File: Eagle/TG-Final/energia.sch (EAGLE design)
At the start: 1 part

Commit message: Comienzo placa potencia
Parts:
- added C1: 470uf, rcl:CPOL-USE3.5-8
- added C2: 0.1uf, rcl:C-EU025-025X050
- added D1: 1N4007, adafruit:1N4004
- added IC1, IC2: 7812T, linear:7812T
- added IC3: 7806T, linear:7806T
- added R1, R2: 1 Ohm 1W, rcl:R-US_0411/15
- added U$8: PIC16F88-DIP, SparkFun:PIC16F88-DIP
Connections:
- net P$1 renamed +11V1
- removed net +24V: U$1.PIN17
- removed net +5V: U$1.PIN20
- new net +22V: R1.1, R2.1, U$1.PIN17
- new net +6V: IC3.VO, U$1.PIN20
- new net N$1: IC2.VI, R2.2
- new net N$2: D1.C, IC1.VI, R1.2
- new net VDD: U$1.PIN21
- net +12V: now also C1.+, C2.1, D1.A, IC1.VO, IC2.VO, IC3.VI
- net +3V3: now also U$1.PIN22; no longer U$1.PIN21
- net VSS: now also C1.-, C2.2, IC1.GND, IC2.GND, IC3.GND

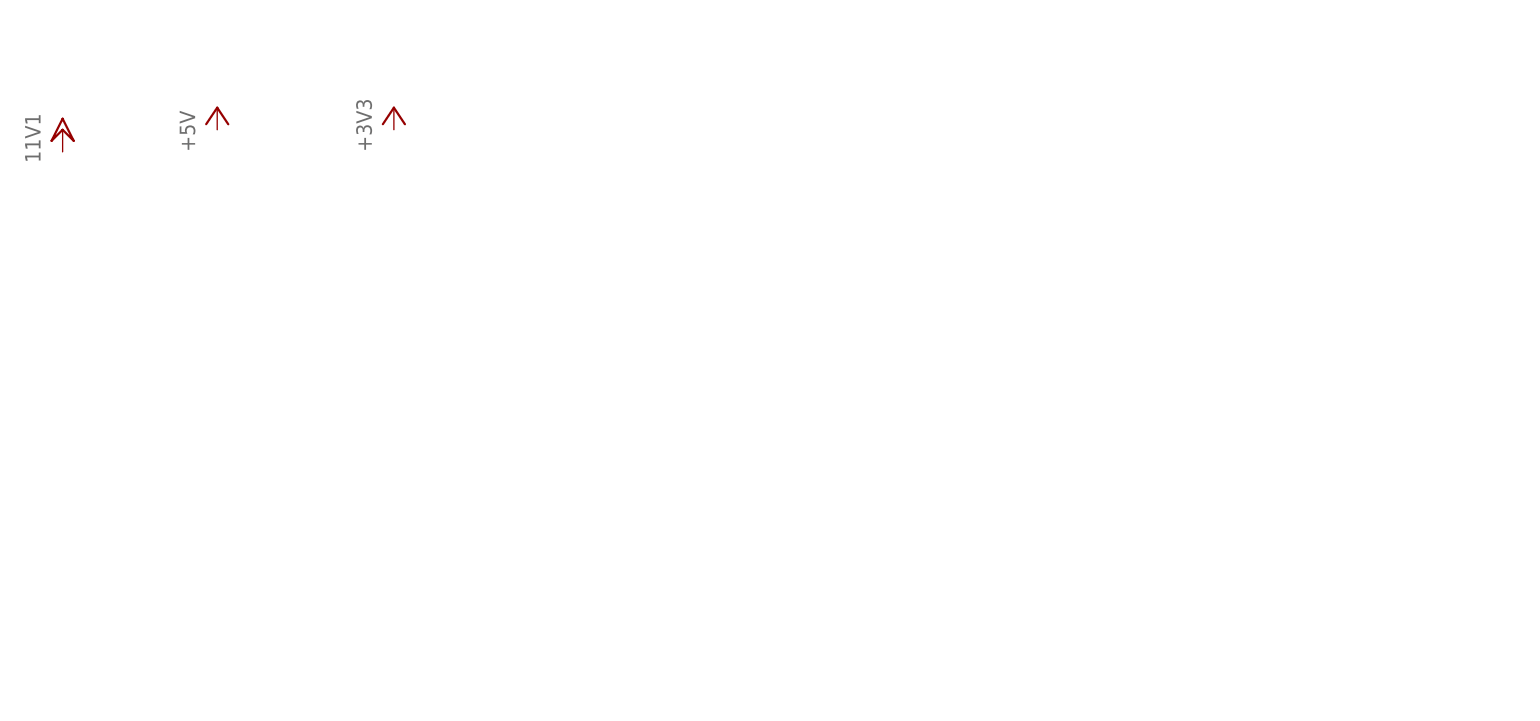
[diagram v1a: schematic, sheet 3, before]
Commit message: Fuente 11.1v -> 5v y 3v3
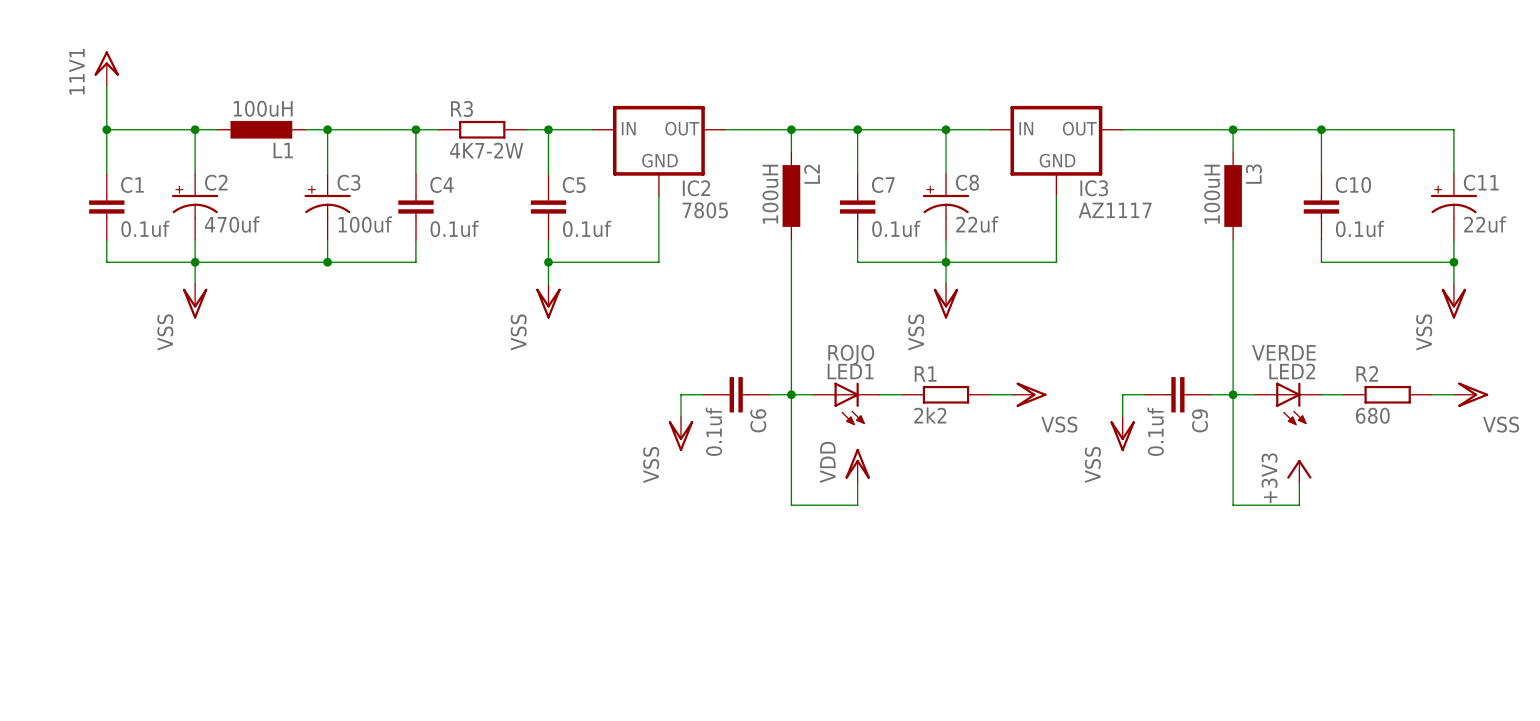
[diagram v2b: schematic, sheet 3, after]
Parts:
- removed D1: 1N4007, adafruit:1N4004
- added C10, C4, C5, C6, C7, C9: 0.1uf, rcl:C-EU050-024X044
- added C11, C8: 22uf, rcl:CPOL-USE2.5-7
- added C3: 100uf, rcl:CPOL-USE2.5-7
- added JP1: (no value), SparkFun:M06LONGPADS
- added L1, L2, L3: 100uH, rcl:L-EU0207/7
- added LED1: ROJO, adafruit:LED3MM
- added LED2: VERDE, adafruit:LED3MM
- added Q1: TIP2955, transistor-power:TIP2955
- added R3: 4K7-2W, rcl:R-EU_0411/12
- C1: value 470uf -> 0.1uf; device rcl:CPOL-USE3.5-8 -> rcl:C-EU050-024X044
- C2: value 0.1uf -> 470uf; device rcl:C-EU025-025X050 -> rcl:CPOL-USE2.5-7
- IC2: value 7812T -> 7805; device linear:7812T -> SparkFun:V_REG_78XX-TO-220
- IC3: value 7806T -> AZ1117; device linear:7806T -> SparkFun:V_REG_LD1117VXX
- R1: value 1 Ohm 1W -> 2k2; device rcl:R-US_0411/15 -> rcl:R-EU_0204/5
- R2: value 1 Ohm 1W -> 680; device rcl:R-US_0411/15 -> rcl:R-EU_0204/5
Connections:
- new net N$10: C5.1, IC2.IN, R3.2
- new net N$11: C3.+, C4.1, L1.2, R3.1
- new net N$12: C7.1, C8.+, IC2.OUT, IC3.IN, L2.2
- new net N$14: LED1.C, R1.1
- new net N$17: C10.1, C11.+, IC3.OUT, L3.2
- new net N$18: LED2.C, R2.1
- new net N$3: JP1.5, U$8.VDD
- new net N$4: JP1.4, U$8.VSS
- new net N$5: JP1.3, U$8.RB7/PGD
- new net N$6: JP1.2, U$8.RB6/PGC
- new net N$7: U$1.PIN15
- new net N$8: U$1.PIN14
- new net N$9: U$1.PIN13
- net +11V1: now also C1.1, C2.+, L1.1
- net +12V: no longer C1.+, C2.1, D1.A, IC1.VO, IC2.VO, IC3.VI
- net +22V: now also IC1.VI, Q1.B, Q1.E; no longer R1.1, R2.1
- net +3V3: now also C9.1, L3.1, LED2.A
- net +6V: no longer IC3.VO
- net N$1: now also IC1.VO, Q1.C; no longer IC2.VI, R2.2
- net N$2: now also JP1.6, U$8.RA5/MCLR; no longer D1.C, IC1.VI, R1.2
- net VDD: now also C6.1, L2.1, LED1.A
- net VSS: now also C1.2, C10.2, C11.-, C2.-, C3.-, C4.2, C5.2, C6.2, C7.2, C8.-, C9.2, R1.2, R2.2; no longer C1.-, C2.2
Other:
- moved on the sheet: IC1, U$8

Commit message: Monitor Baterias LiPO
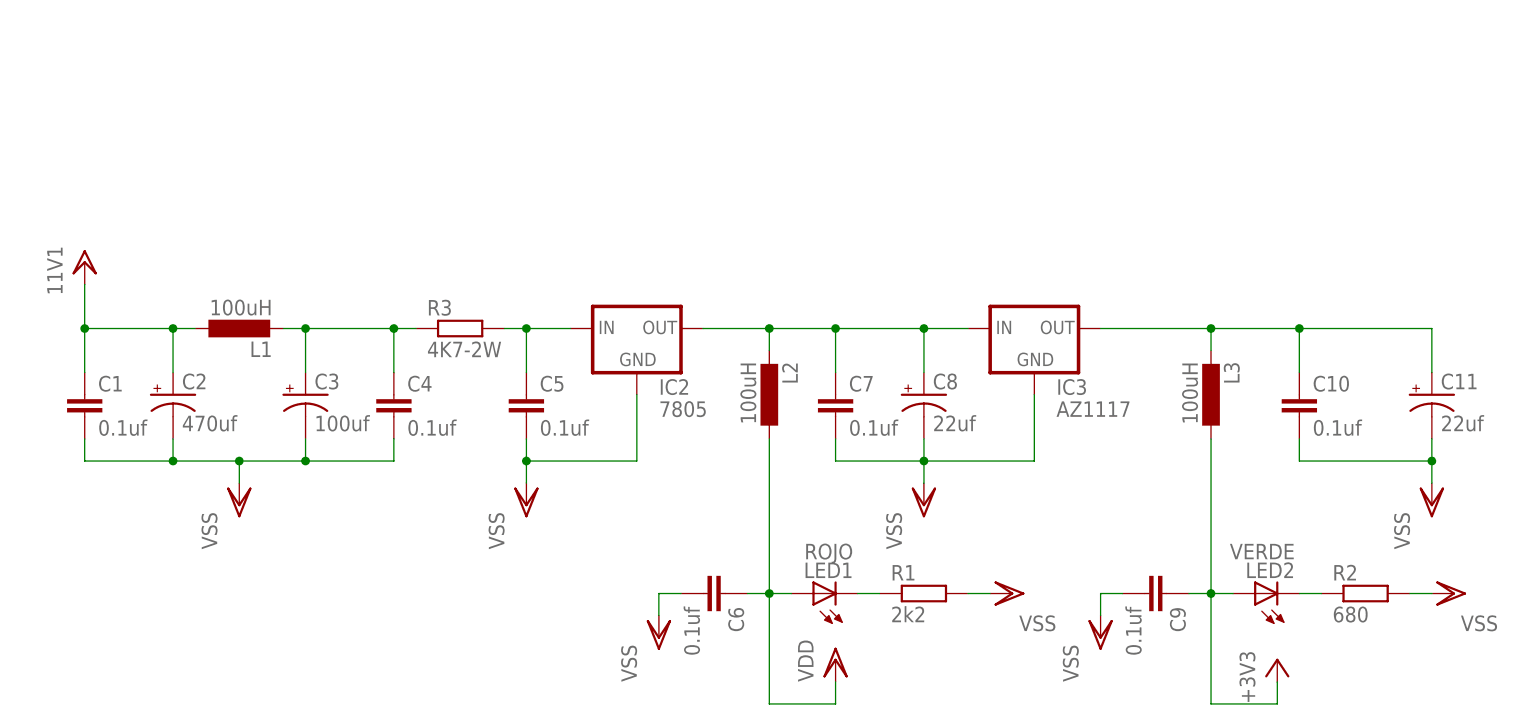
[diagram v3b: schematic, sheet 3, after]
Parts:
- removed IC1: 7812T, linear:7812T
- removed Q1: TIP2955, transistor-power:TIP2955
- added R4: 1k, rcl:R-EU_0204/5
- JP1: value (none) -> (none)
- renumbered U$8 to MONITORBATERIA
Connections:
- removed net N$1: IC1.VO, Q1.C
- removed net N$3: JP1.5, MONITORBATERIA.VDD
- removed net N$4: JP1.4, MONITORBATERIA.VSS
- removed net N$7: U$1.PIN15
- removed net N$8: U$1.PIN14
- removed net N$9: U$1.PIN13
- new net SENSE1: MONITORBATERIA.RA0/AN0, U$1.PIN15
- new net SENSE2: MONITORBATERIA.RA1/AN1, U$1.PIN13
- new net SENSE3: MONITORBATERIA.RA2/AN2, U$1.PIN14
- net +22V: no longer IC1.VI, Q1.B, Q1.E
- net VDD: now also JP1.5, MONITORBATERIA.VDD, R4.1
- net VSS: now also JP1.4, MONITORBATERIA.VSS, R4.2; no longer IC1.GND
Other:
- moved on the sheet: C1, C10, C11, C2, C3, C4, C5, C6, C7, C8, C9, IC2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

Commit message: Fuente de Potencia
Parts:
- removed R3: 4K7-2W, rcl:R-EU_0411/12
- added C12: 3300uf, rcl:CPOL-USE7.5-18
- added C13, C15: 470uf, rcl:CPOL-USE3.5-8
- added C14: 10uf, rcl:CPOL-USE2.5-5
- added C16, C17: 0.1uf, rcl:C-EU050-024X044
- added D1: 1N4007, diode:1N4004
- added IC1: 7812T, adafruit:7812T
- added IC4: 7806T, adafruit:7806T
- added Q1: TIP2955, transistor-power:TIP2955
- added R5: 2W100R, rcl:R-EU_0411/12
- added S1: SWITCH-2-ESTADOS, aasanchez:TL39YOSWITCH_2_ESTADOS
- added S2: SWITCH, aasanchez:TL39YOSWITCH_2_ESTADOS
- added U$6: 5W0.1RJ, aasanchez:RESISTENCIA5WATT
- added U$9: 10W 5R6J, aasanchez:RESISTENCIA10W
- L1: device rcl:L-EU0207/7 -> rcl:L-EUTFI0307
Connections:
- new net N$1: C1.1, C2.+, L1.1, S1.P
- new net N$13: C15.+, C16.1, D1.C, IC4.VI
- new net N$4: C12.+, R5.1, S2.P, U$6.P$1
- new net N$7: Q1.E, U$6.P$2
- new net N$8: C13.+, IC1.VI, Q1.B, R5.2
- net +11V1: now also S1.O; no longer C1.1, C2.+, L1.1
- net +12V: now also C14.+, D1.A, IC1.VO, Q1.C
- net +22V: now also S2.O
- net +6V: now also C17.1, IC4.VO
- net N$10: now also U$9.P$2; no longer R3.2
- net N$11: now also U$9.P$1; no longer R3.1
- net VSS: now also C12.-, C13.-, C14.-, C15.-, C16.2, C17.2, IC1.GND, IC4.GND

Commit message: Trabajos en la Sub Estacion
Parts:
- added C18, C19: 0.1uf, rcl:C-EU050-024X044
- added LED3: ROJO, adafruit:LED3MM
- added LED4: VERDE, adafruit:LED3MM
- added R3: 2k2, rcl:R-EU_0204/5
- added R6: 680, rcl:R-EU_0204/5
- S1: value SWITCH-2-ESTADOS -> SWITCH
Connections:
- new net N$3: LED3.C, R3.1
- new net N$9: LED4.C, R6.1
- net +11V1: now also S1.S; no longer S1.O
- net +12V: now also C18.1, LED3.A
- net +6V: now also C19.1, LED4.A
- net VSS: now also C18.2, C19.2, R3.2, R6.2

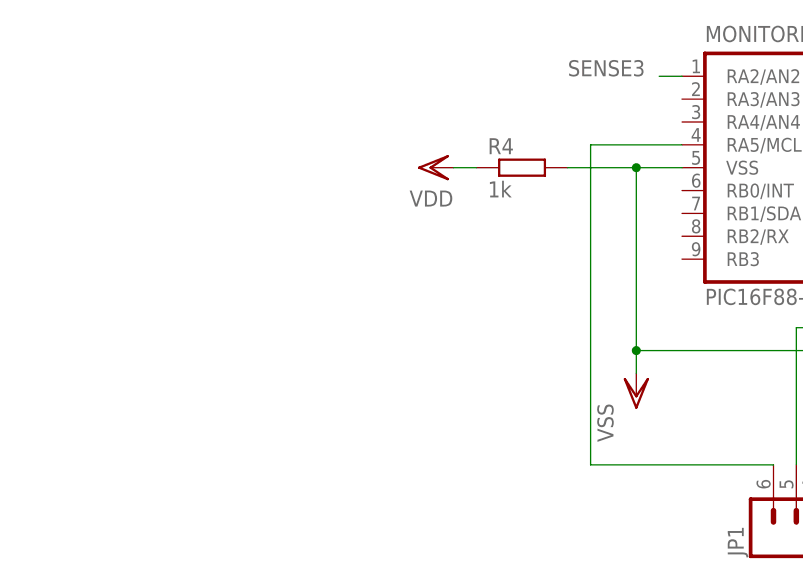
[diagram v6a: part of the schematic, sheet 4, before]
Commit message: Pruebas del Monitor de Baterias Lipo
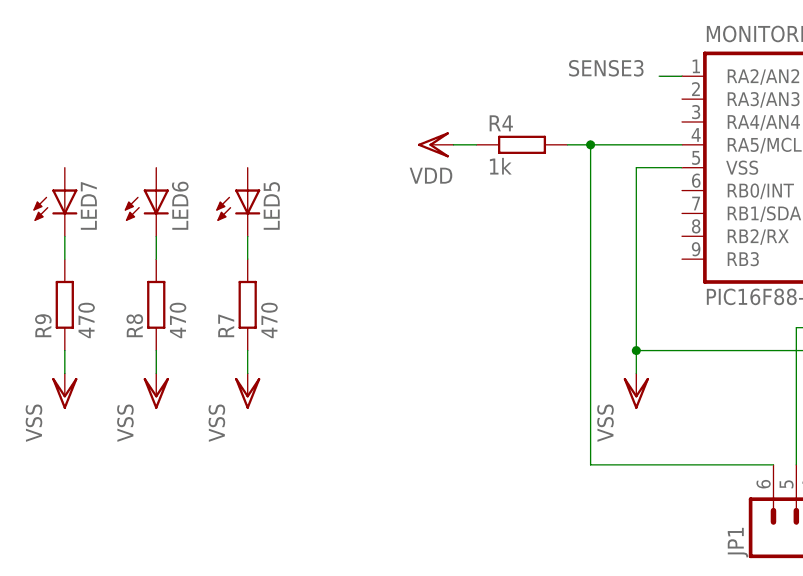
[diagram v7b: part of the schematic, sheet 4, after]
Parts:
- added LED5, LED6, LED7: (no value), adafruit:LED3MM
- added R7, R8, R9: 470, rcl:R-EU_0204/5
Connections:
- new net N$15: LED5.C, R7.2
- new net N$16: LED6.C, R8.2
- new net N$19: LED7.C, R9.2
- net N$2: now also R4.2
- net VSS: now also R7.1, R8.1, R9.1; no longer R4.2
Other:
- moved on the sheet: R4

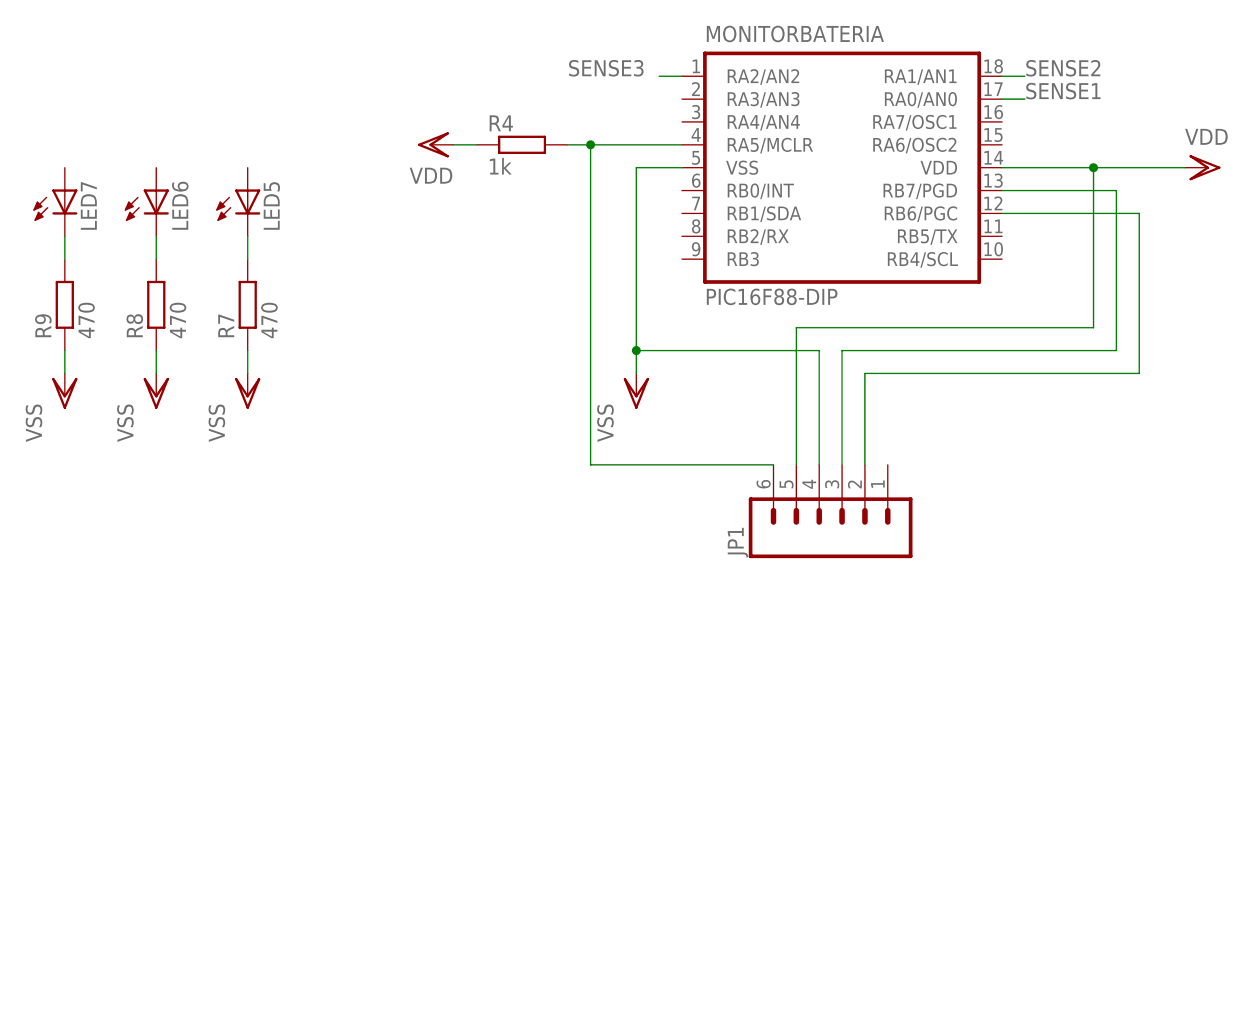
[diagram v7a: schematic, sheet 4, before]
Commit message: Peliando con un 16f88
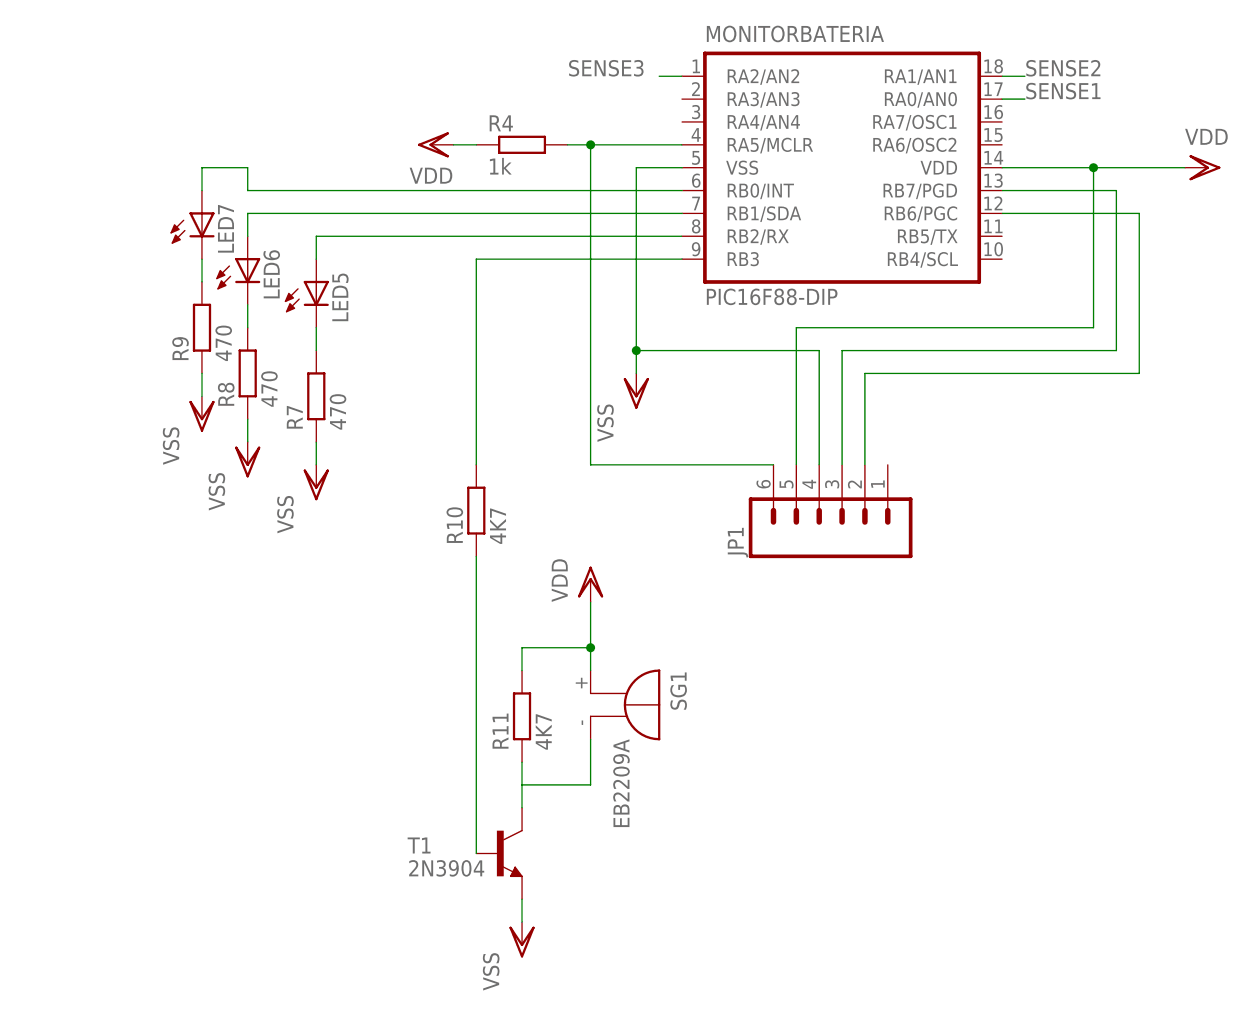
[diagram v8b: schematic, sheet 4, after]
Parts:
- added R10: 4K7, rcl:R-EU_0207/10
- added R11: 4K7, rcl:R-EU_0204/5
- added SG1: EB2209A, buzzer:EB2209A
- added T1: 2N3904, transistor:2N3904
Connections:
- new net N$20: LED7.A, MONITORBATERIA.RB0/INT
- new net N$21: LED6.A, MONITORBATERIA.RB1/SDA
- new net N$22: LED5.A, MONITORBATERIA.RB2/RX
- new net N$23: MONITORBATERIA.RB3, R10.2
- new net N$24: R10.1, T1.B
- new net N$25: R11.1, SG1.-, T1.C
- net VDD: now also R11.2, SG1.+
- net VSS: now also T1.E
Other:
- moved on the sheet: LED5, LED6, LED7, R7, R8, R9
